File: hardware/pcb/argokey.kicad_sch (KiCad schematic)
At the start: 174 parts, among them J1 USB_BOOT, J2 USB_C_Receptacle_USB2.0, SW1 RotaryEncoder_Switch, SW2 RESET, U1 W25Q16JVSSIQ, U2 RP2040, U3 NCP1117-3.3_SOT223, Y1 ABLS-12.000MHZ-B4-T

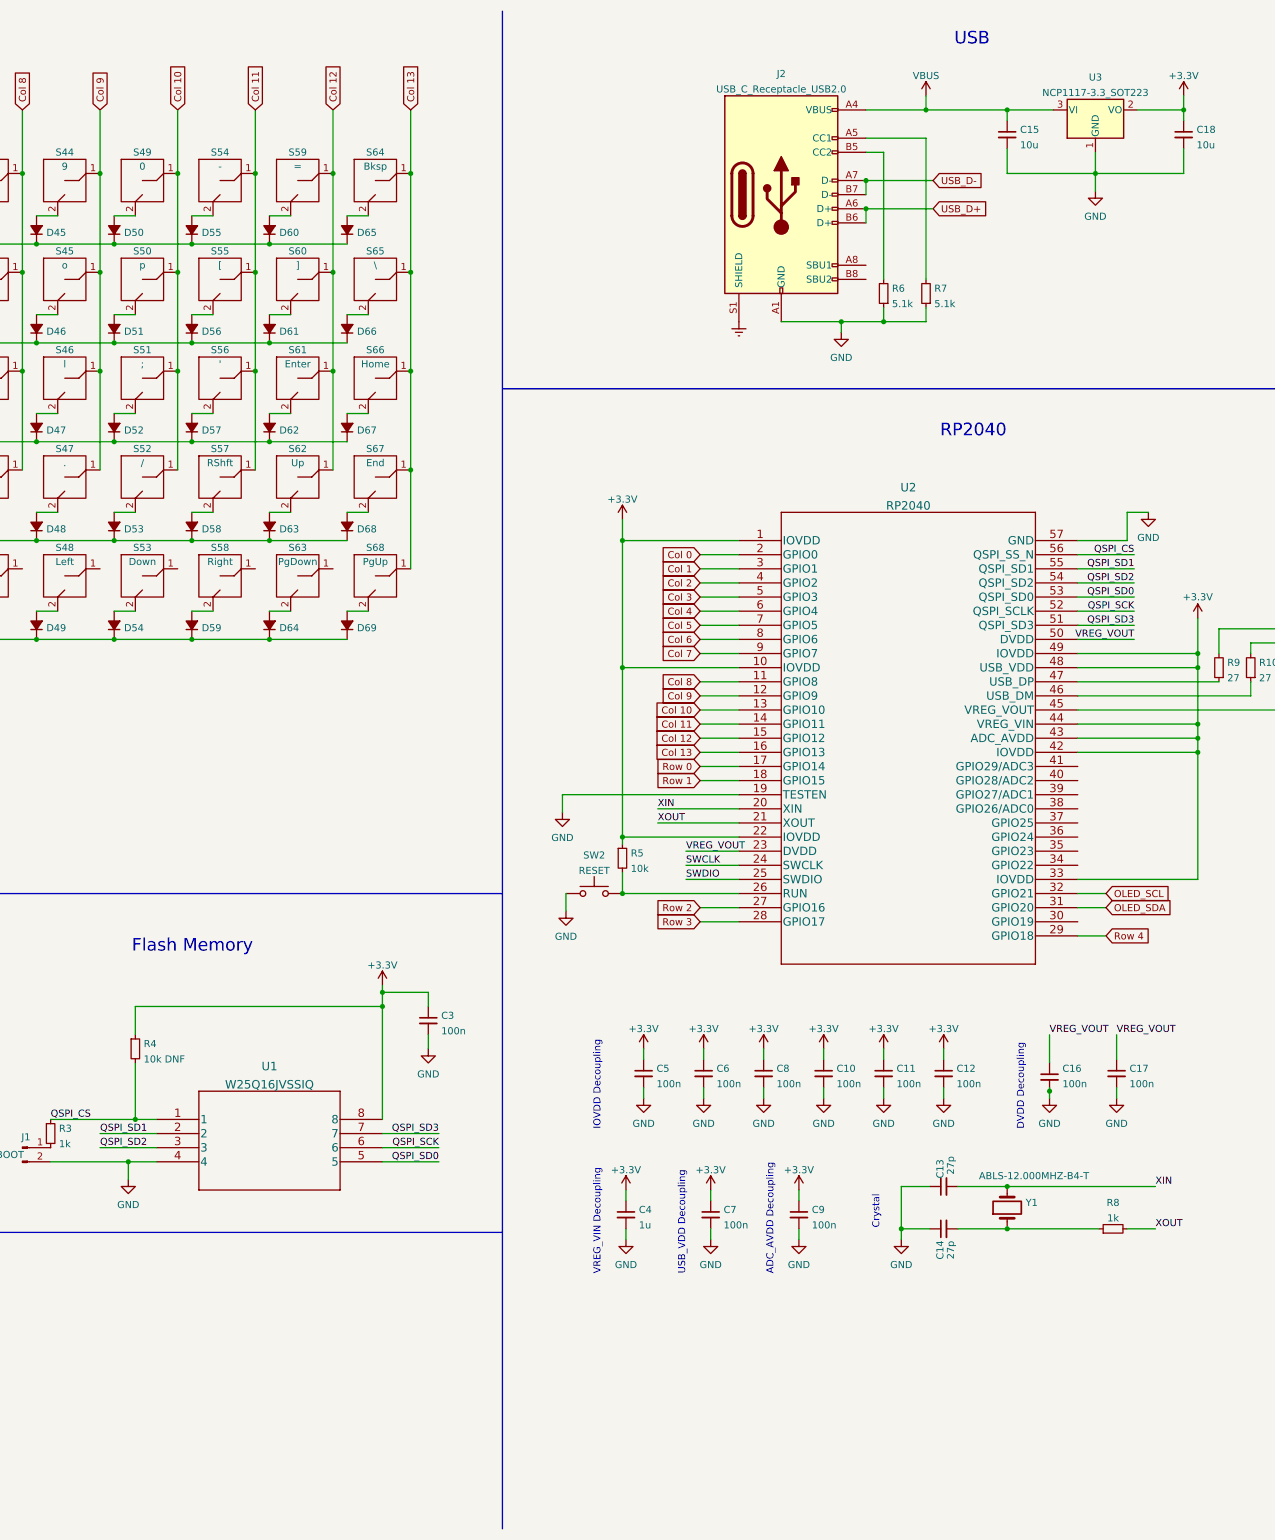
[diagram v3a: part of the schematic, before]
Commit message: Sch: Add connectors
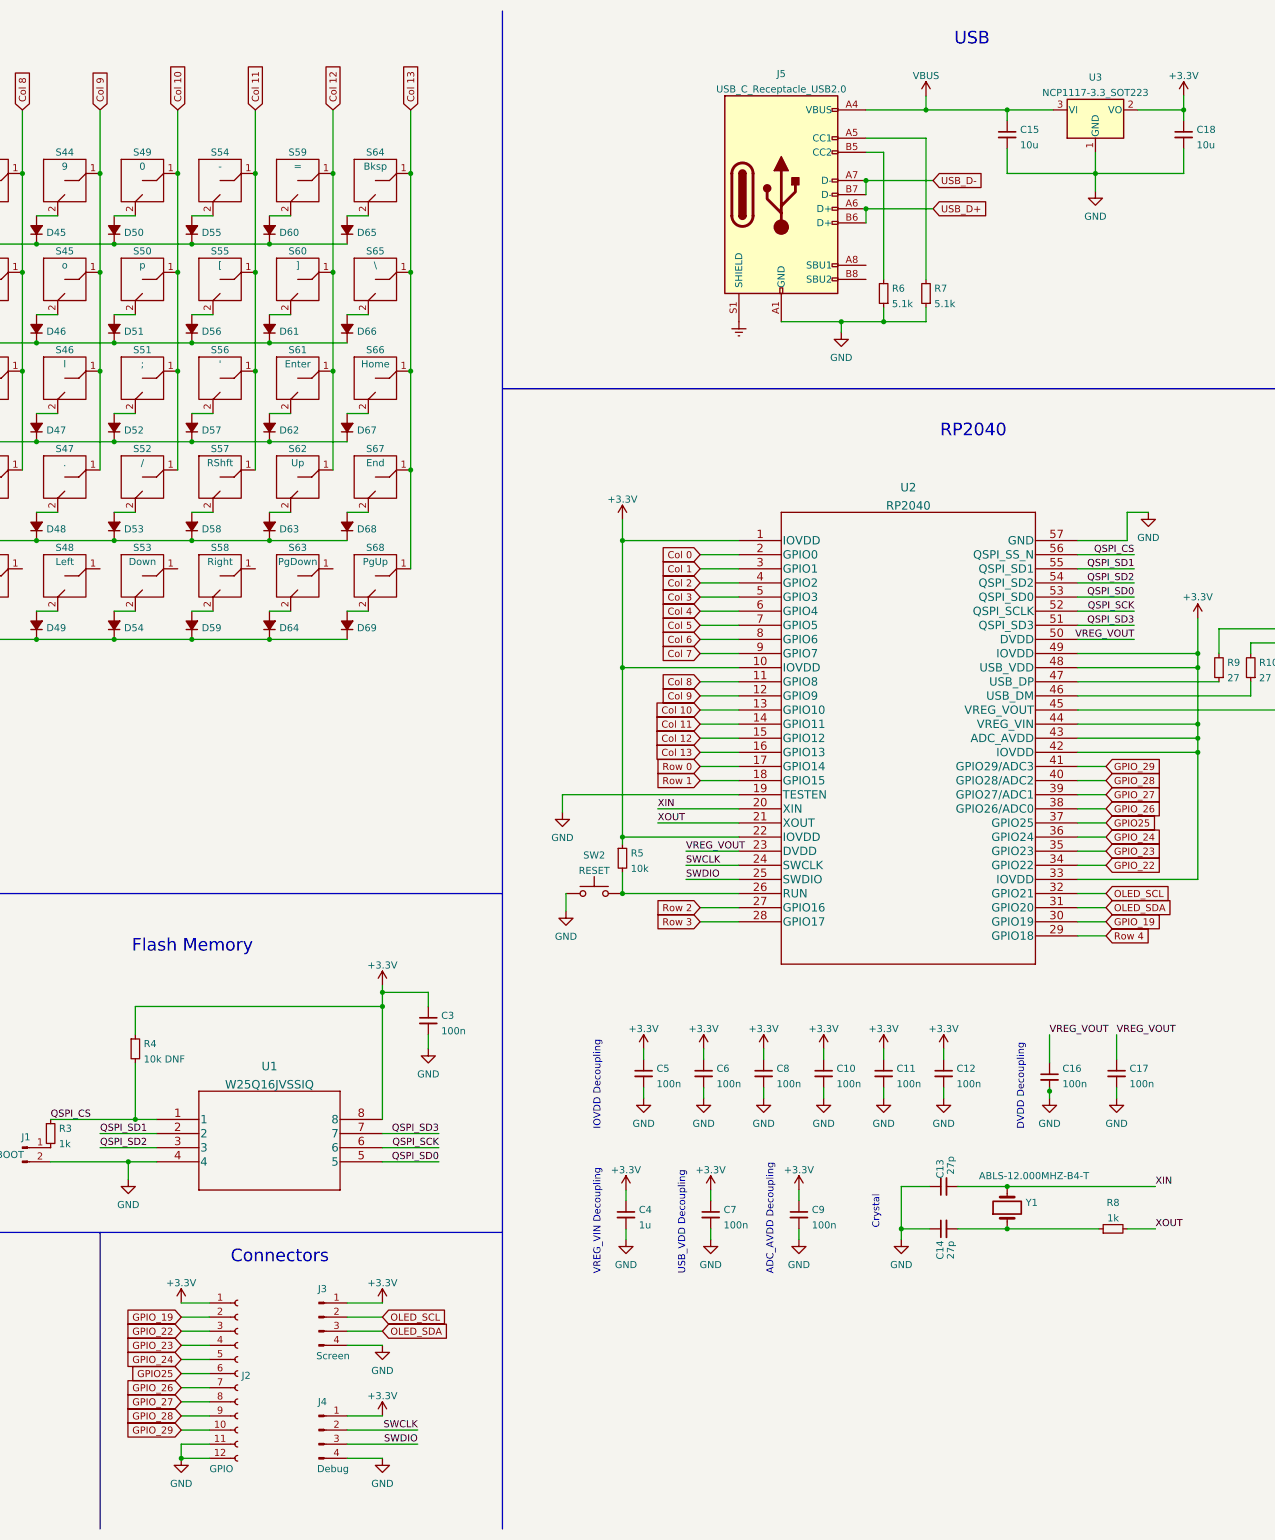
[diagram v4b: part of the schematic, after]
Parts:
- added J2: GPIO, symbol Connector:Conn_01x12_Female
- added J3: Screen, symbol Connector:Conn_01x04_Male
- added J4: Debug, symbol Connector:Conn_01x04_Male
- renumbered J2 to J5
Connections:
- net +3V3: now also J2.1 (Pin_1), J3.1 (Pin_1), J4.1 (Pin_1)
- net GND: now also J2.11 (Pin_11), J2.12 (Pin_12), J3.4 (Pin_4), J4.4 (Pin_4)
- net OLED_SCL: now also J3.2 (Pin_2)
- net OLED_SDA: now also J3.3 (Pin_3)
- net SWCLK: now also J4.2 (Pin_2)
- net SWDIO: now also J4.3 (Pin_3)
- net GPIO_19: now reaches U2.30 (GPIO19)
- net GPIO_19: now also J2.2 (Pin_2)
- net GPIO_22: now reaches U2.34 (GPIO22)
- net GPIO_22: now also J2.3 (Pin_3)
- net GPIO_23: now reaches U2.35 (GPIO23)
- net GPIO_23: now also J2.4 (Pin_4)
- net GPIO_24: now reaches U2.36 (GPIO24)
- net GPIO_24: now also J2.5 (Pin_5)
- net GPIO25: now reaches U2.37 (GPIO25)
- net GPIO25: now also J2.6 (Pin_6)
- net GPIO_26: now reaches U2.38 (GPIO26/ADC0)
- net GPIO_26: now also J2.7 (Pin_7)
- net GPIO_27: now reaches U2.39 (GPIO27/ADC1)
- net GPIO_27: now also J2.8 (Pin_8)
- net GPIO_28: now reaches U2.40 (GPIO28/ADC2)
- net GPIO_28: now also J2.9 (Pin_9)
- net GPIO_29: now reaches U2.41 (GPIO29/ADC3)
- net GPIO_29: now also J2.10 (Pin_10)
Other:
- note added: "Connectors"

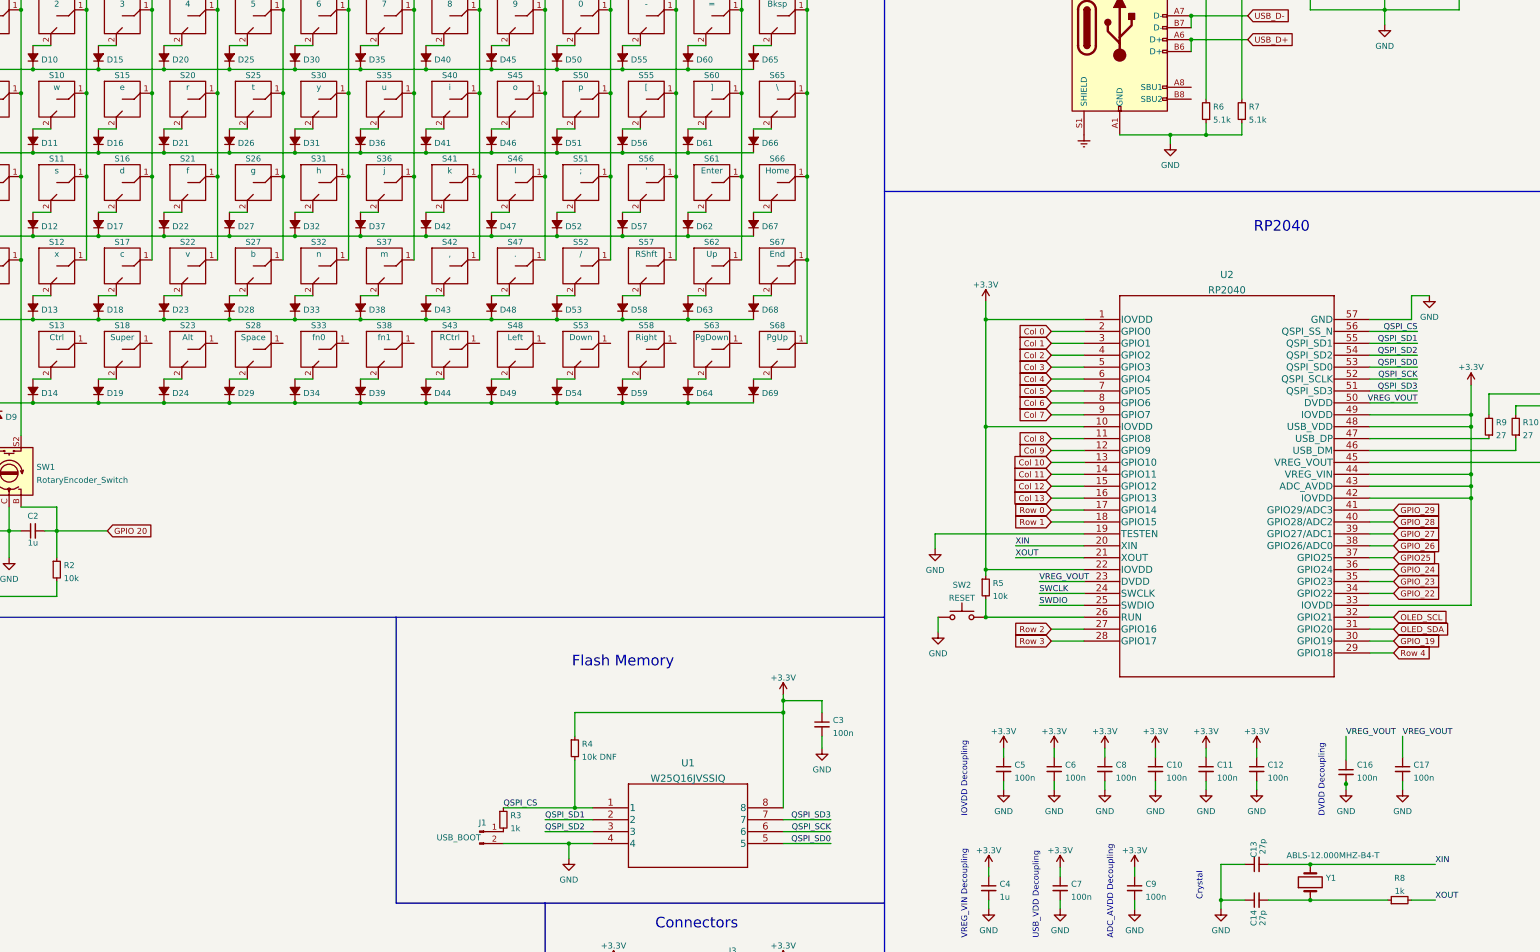
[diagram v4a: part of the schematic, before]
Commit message: Sch: Replace Flash, Mark Non-con
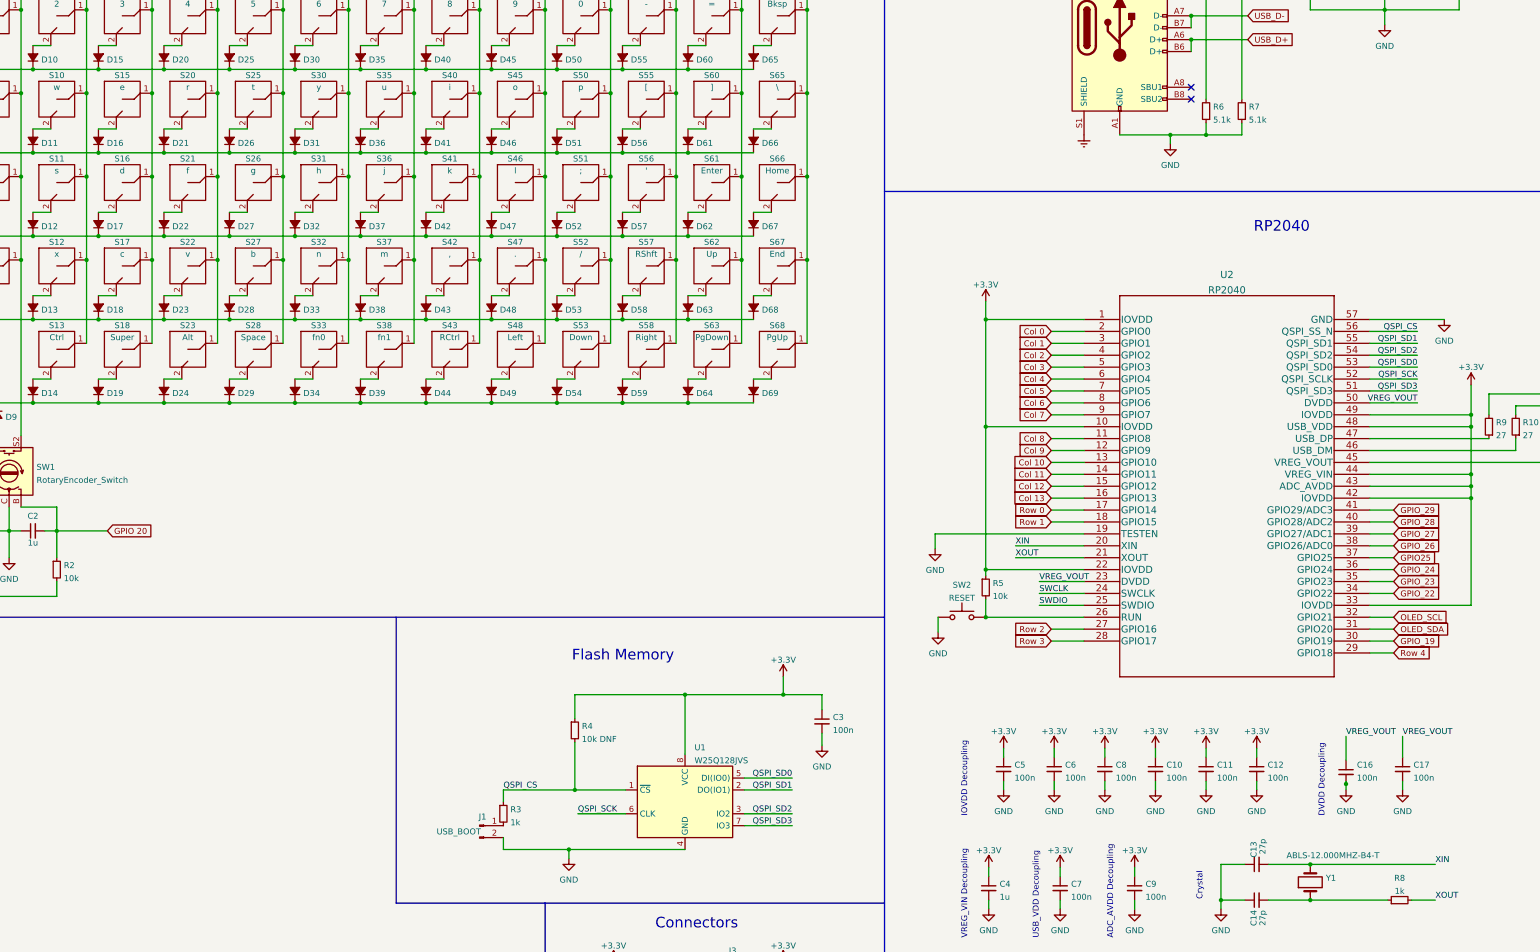
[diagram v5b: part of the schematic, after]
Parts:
- removed U1: W25Q16JVSSIQ, W25Q16JVSSIQ_WIN, symbol W25Q16JVSSIQ:W25Q16JVSSIQ
- added U1: W25Q128JVS, Package_SO:SOIC-8_5.23x5.23mm_P1.27mm, symbol Memory_Flash:W25Q128JVS
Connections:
- net +3V3: now also U1.8 (VCC)
- net Col 10: now also S53.1
- net Col 11: now also S58.1
- net Col 12: now also S63.1
- net Col 2: now also S13.1
- net Col 3: now also S18.1
- net Col 4: now also S23.1
- net Col 5: now also S28.1
- net Col 6: now also S33.1
- net Col 7: now also S38.1
- net Col 8: now also S43.1
- net Col 9: now also S48.1
- net GND: now also U1.4 (GND)
- net QSPI_CS: now also U1.1 (~{CS})
- net QSPI_SCK: now also U1.6 (CLK)
- net QSPI_SD0: now also U1.5 (DI(IO0))
- net QSPI_SD1: now also U1.2 (DO(IO1))
- net QSPI_SD2: now also U1.3 (IO2)
- net QSPI_SD3: now also U1.7 (IO3)
- no-connect marks 0 -> 2
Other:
- moved on the sheet: C3, J1, R3, R4

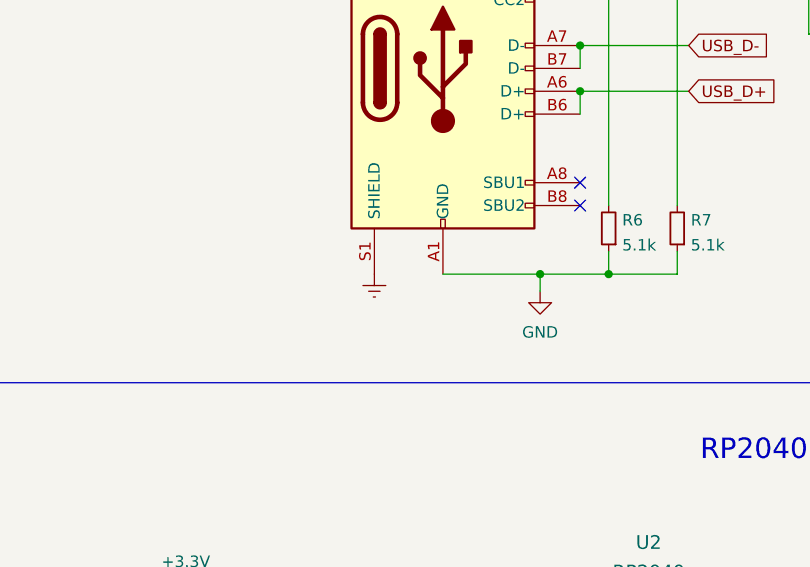
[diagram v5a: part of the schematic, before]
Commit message: Sch: Set USB GND VBUS power output
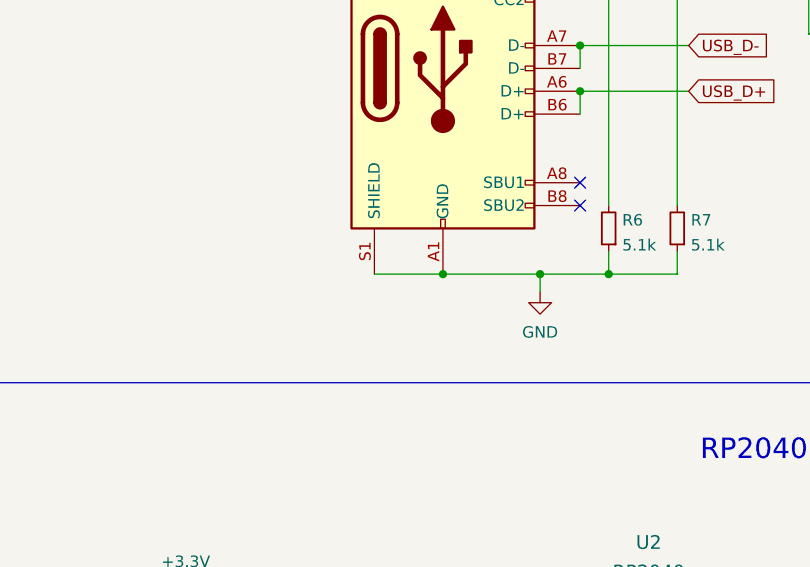
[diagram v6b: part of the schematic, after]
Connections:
- net Earth is gone; now on net GND: J5.S1 (SHIELD)
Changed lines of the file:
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@@
   (junction (at 171.45 59.055) (diameter 0) (color 0 0 0 0)
   )
+  (junction (at 294.005 67.945) (diameter 0) (color 0 0 0 0)
+  )
   (junction (at 87.63 94.615) (diameter 0) (color 0 0 0 0)
   )
@@
     (stroke (width 0) (type default) (color 0 0 0 0))
   )
+  (wire (pts (xy 286.385 67.945) (xy 294.005 67.945))
+    (stroke (width 0) (type default) (color 0 0 0 0))
+  )
   (wire (pts (xy 187.96 84.455) (xy 191.77 84.455))
     (stroke (width 0) (type default) (color 0 0 0 0))
@@
     (pin "2")
   )
-  (symbol (lib_id "power:Earth") (at 286.385 67.945 0) (unit 1)
-    (in_bom yes) (on_board yes) (fields_autoplaced)
-    (property "Reference" "#PWR023" (id 0) (at 286.385 74.295 0)
-      (effects (font (size 1.27 1.27)) hide)
-    )
-    (property "Value" "Earth" (id 1) (at 286.385 71.755 0)
-      (effects (font (size 1.27 1.27)) hide)
-    )
-    (property "Footprint" "" (id 2) (at 286.385 67.945 0)
-      (effects (font (size 1.27 1.27)) hide)
-    )
-    (property "Datasheet" "~" (id 3) (at 286.385 67.945 0)
-      (effects (font (size 1.27 1.27)) hide)
-    )
-    (pin "1")
-  )
   (symbol (lib_id "Device:D_Small_Filled") (at 215.9 69.215 90) (unit 1)
     (in_bom yes) (on_board yes) (fields_autoplaced)
@@
       (reference "#PWR022") (unit 1) (value "GND") (footprint "")
     )
-    (path "/aeb8cba0-ba15-495c-8dc2-79e706efb28f"
-      (reference "#PWR023") (unit 1) (value "Earth") (footprint "")
-    )
     (path "/815d0923-6bf9-4220-8d6c-9e00f77614c4"
